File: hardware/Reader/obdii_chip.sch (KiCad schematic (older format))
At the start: 23 parts

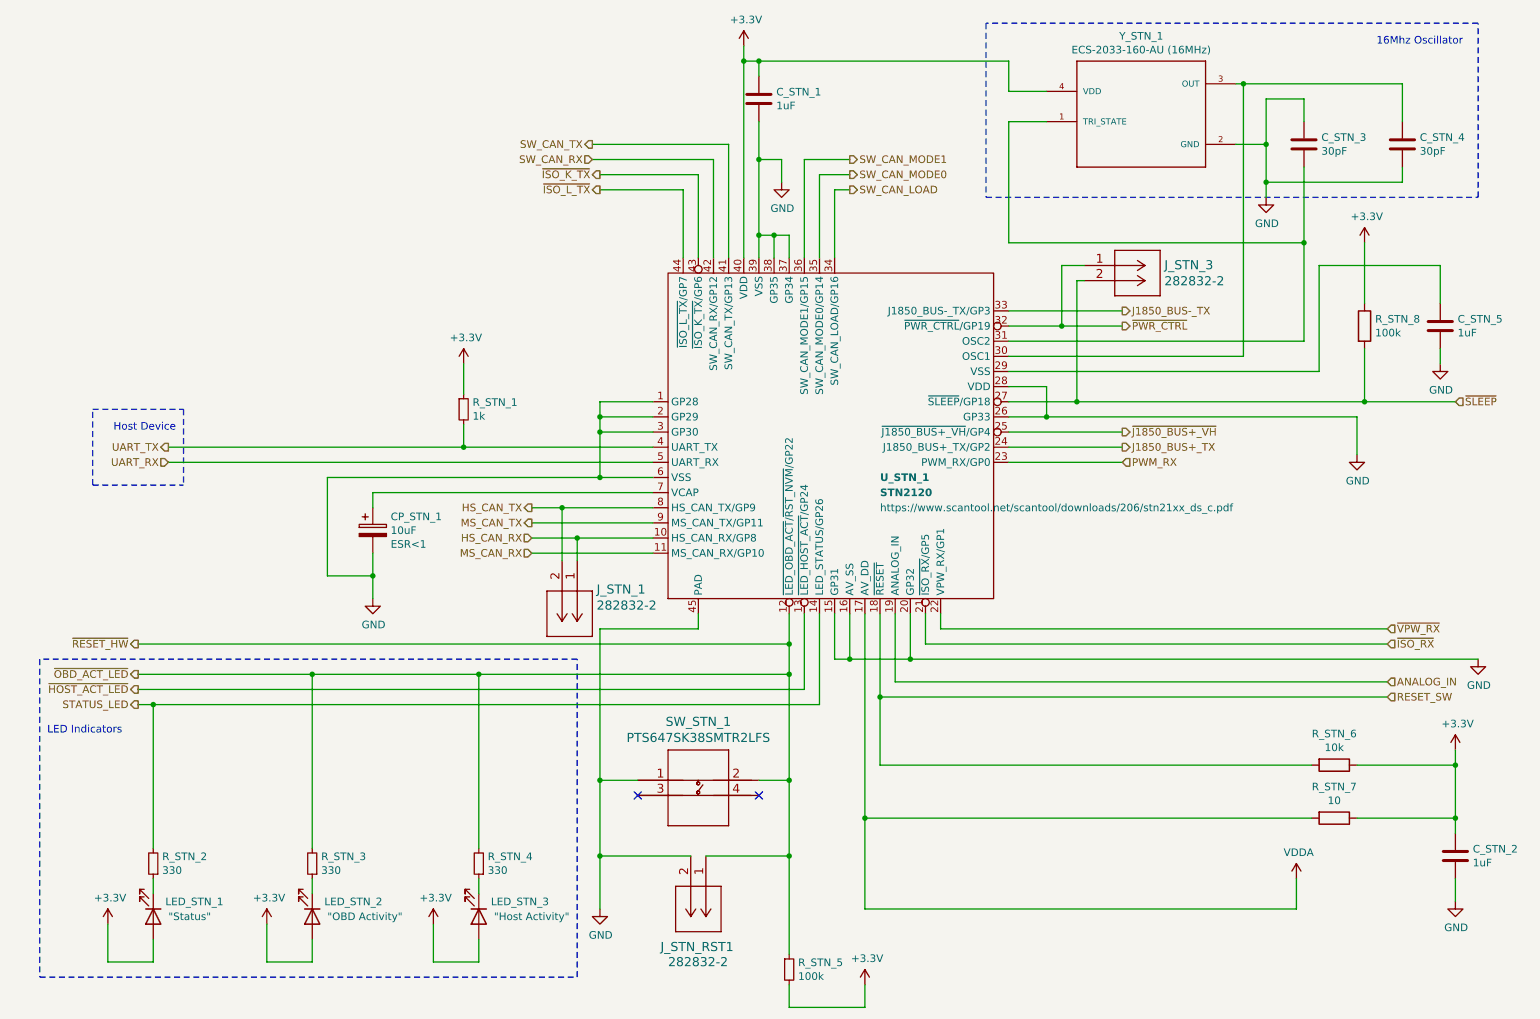
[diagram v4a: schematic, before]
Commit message: Fixed wiring issue on ESD Protection
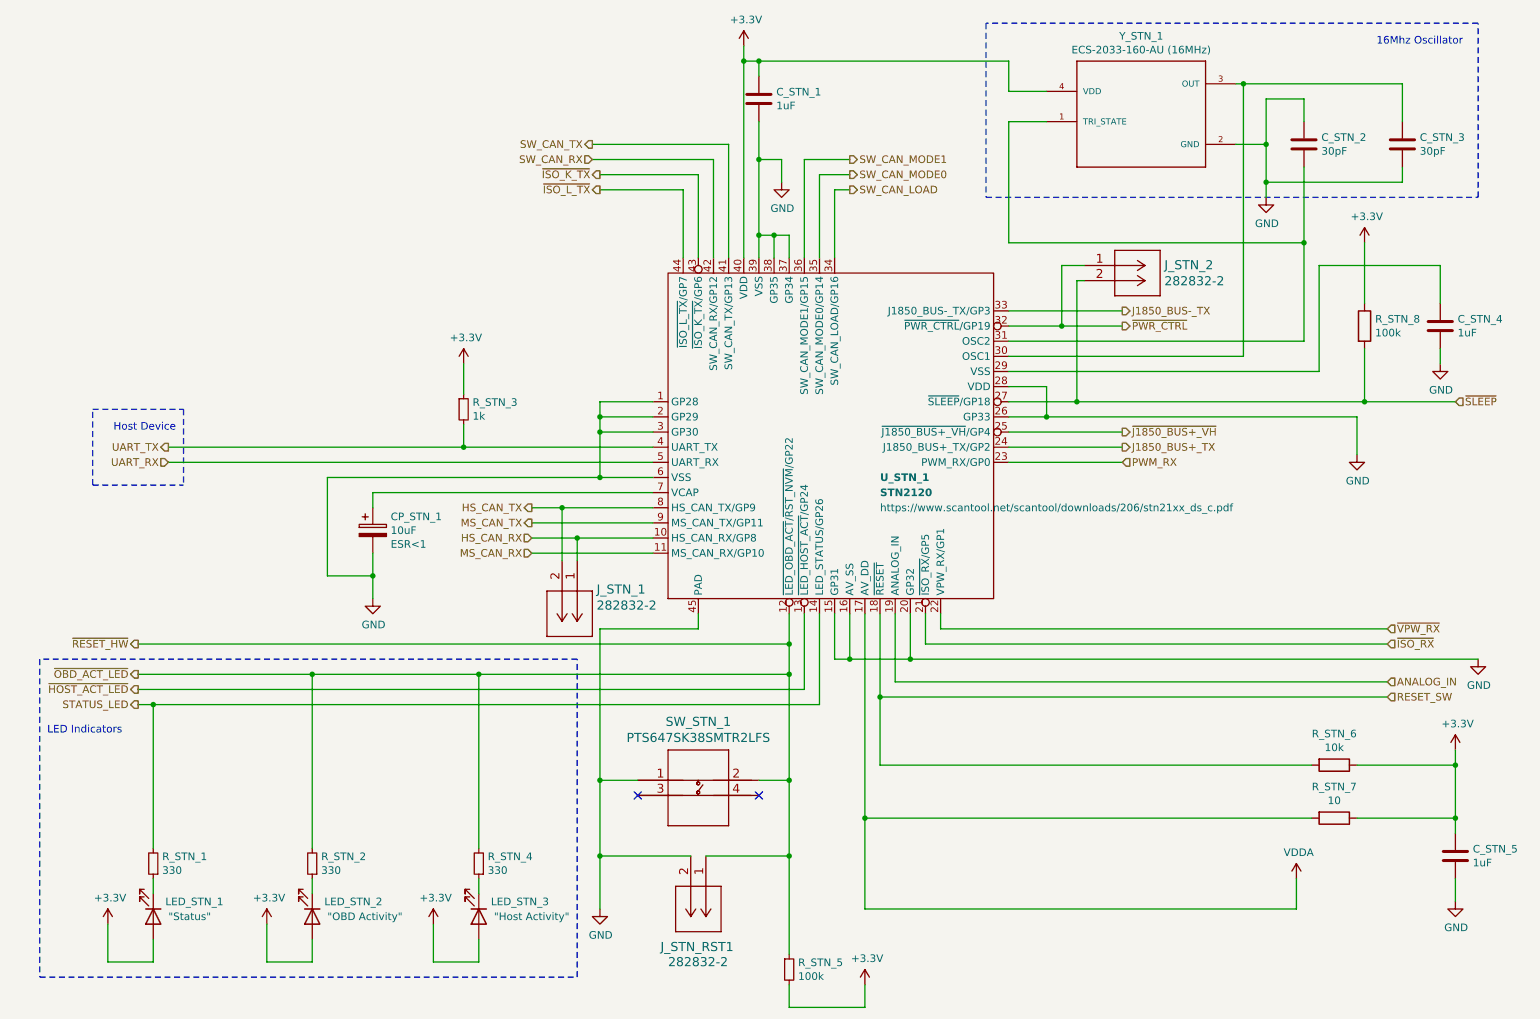
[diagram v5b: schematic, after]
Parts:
- renumbered C_STN_3 to C_STN_2, C_STN_4 to C_STN_3, C_STN_5 to C_STN_4, C_STN_2 to C_STN_5, J_STN_3 to J_STN_2, R_STN_2 to R_STN_1, R_STN_3 to R_STN_2, R_STN_1 to R_STN_3
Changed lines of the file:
@@
 $EndDescr
 $Comp
-L CANtech:STN2120 U?
+L CANtech:STN2120 U_STN_?
 U 1 1 5FC0708B
 P 6050 3350
-AR Path="/5F95F80B/5FC0708B" Ref="U?"  Part="1"
+AR Path="/5F95F80B/5FC0708B" Ref="U_STN_?"  Part="1"
 AR Path="/5F95F80B/5FC0631B/5FC0708B" Ref="U_STN_1"  Part="1"
 F 0 "U_STN_1" H 6250 3000 50  0000 L CNB
@@
 $EndComp
 $Comp
-L Device:R_Small R_STN_1
+L Device:R_Small R_STN_3
 U 1 1 5FC0B04F
 P 3500 3250
-F 0 "R_STN_1" H 3559 3296 50  0000 L CNN
+F 0 "R_STN_3" H 3559 3296 50  0000 L CNN
 F 1 "1k" H 3559 3205 50  0000 L CNN
 F 2 "footprints:RC1608F102CS" H 3500 3250 50  0001 C CNN
@@
 UART_RX
 $Comp
-L power:+3.3V #PWR0192
+L power:+3.3V #PWR060
 U 1 1 5FC0B98A
 P 3500 2950
-F 0 "#PWR0192" H 3500 2800 50  0001 C CNN
+F 0 "#PWR060" H 3500 2800 50  0001 C CNN
 F 1 "+3.3V" H 3515 3123 50  0000 C CNN
 F 2 "" H 3500 2950 50  0001 C CNN
@@
 	4400 3400 4400 3700
 $Comp
-L power:GND #PWR0193
+L power:GND #PWR058
 U 1 1 5FC0D5B0
 P 2900 4500
-F 0 "#PWR0193" H 2900 4250 50  0001 C CNN
+F 0 "#PWR058" H 2900 4250 50  0001 C CNN
 F 1 "GND" H 2905 4327 50  0000 C CNN
 F 2 "" H 2900 4500 50  0001 C CNN
@@
 MS_CAN_RX
 $Comp
-L power:GND #PWR0194
+L power:GND #PWR061
 U 1 1 5FC1071B
 P 4400 6550
-F 0 "#PWR0194" H 4400 6300 50  0001 C CNN
+F 0 "#PWR061" H 4400 6300 50  0001 C CNN
 F 1 "GND" H 4405 6377 50  0000 C CNN
 F 2 "" H 4400 6550 50  0001 C CNN
@@
 $EndComp
 $Comp
-L power:+3.3V #PWR0195
+L power:+3.3V #PWR064
 U 1 1 5FC11757
 P 6150 7050
-F 0 "#PWR0195" H 6150 6900 50  0001 C CNN
+F 0 "#PWR064" H 6150 6900 50  0001 C CNN
 F 1 "+3.3V" H 6165 7223 50  0000 C CNN
 F 2 "" H 6150 7050 50  0001 C CNN
@@
 $EndComp
 $Comp
-L Device:R_Small R_STN_3
+L Device:R_Small R_STN_2
 U 1 1 5FC13627
 P 2500 6250
-F 0 "R_STN_3" H 2441 6204 50  0000 R CNN
+F 0 "R_STN_2" H 2441 6204 50  0000 R CNN
 F 1 "330" H 2441 6295 50  0000 R CNN
 F 2 "footprints:RESC3216X70N" H 2500 6250 50  0001 C CNN
@@
 	2500 6350 2500 6450
 $Comp
-L power:+3.3V #PWR0196
+L power:+3.3V #PWR057
 U 1 1 5FC1B34E
 P 2200 6650
-F 0 "#PWR0196" H 2200 6500 50  0001 C CNN
+F 0 "#PWR057" H 2200 6500 50  0001 C CNN
 F 1 "+3.3V" H 2215 6823 50  0000 C CNN
 F 2 "" H 2200 6650 50  0001 C CNN
@@
 $EndComp
 $Comp
-L Device:R_Small R_STN_2
+L Device:R_Small R_STN_1
 U 1 1 5FC2D134
 P 1450 6250
-F 0 "R_STN_2" H 1391 6204 50  0000 R CNN
+F 0 "R_STN_1" H 1391 6204 50  0000 R CNN
 F 1 "330" H 1391 6295 50  0000 R CNN
 F 2 "footprints:RESC3216X70N" H 1450 6250 50  0001 C CNN
@@
 	1450 6350 1450 6450
 $Comp
-L power:+3.3V #PWR0197
+L power:+3.3V #PWR056
 U 1 1 5FC2D13B
 P 1150 6650
-F 0 "#PWR0197" H 1150 6500 50  0001 C CNN
+F 0 "#PWR056" H 1150 6500 50  0001 C CNN
 F 1 "+3.3V" H 1165 6823 50  0000 C CNN
 F 2 "" H 1150 6650 50  0001 C CNN
@@
 	3600 6350 3600 6450
 $Comp
-L power:+3.3V #PWR0198
+L power:+3.3V #PWR059
 U 1 1 5FC46408
 P 3300 6650
-F 0 "#PWR0198" H 3300 6500 50  0001 C CNN
+F 0 "#PWR059" H 3300 6500 50  0001 C CNN
 F 1 "+3.3V" H 3315 6823 50  0000 C CNN
 F 2 "" H 3300 6650 50  0001 C CNN
@@
 LED Indicators
 $Comp
-L power:GND #PWR0199
+L power:GND #PWR072
 U 1 1 5FC652FD
 P 10200 4900
-F 0 "#PWR0199" H 10200 4650 50  0001 C CNN
+F 0 "#PWR072" H 10200 4650 50  0001 C CNN
 F 1 "GND" H 10205 4727 50  0000 C CNN
 F 2 "" H 10200 4900 50  0001 C CNN
@@
 	7100 3600 7850 3600
 $Comp
-L power:GND #PWR0203
+L power:GND #PWR067
 U 1 1 5FCB385E
 P 9400 3550
-F 0 "#PWR0203" H 9400 3300 50  0001 C CNN
+F 0 "#PWR067" H 9400 3300 50  0001 C CNN
 F 1 "GND" H 9405 3377 50  0000 C CNN
 F 2 "" H 9400 3550 50  0001 C CNN
@@
 $EndComp
 $Comp
-L power:+3.3V #PWR0204
+L power:+3.3V #PWR068
 U 1 1 5FCC6E89
 P 9450 2150
-F 0 "#PWR0204" H 9450 2000 50  0001 C CNN
+F 0 "#PWR068" H 9450 2000 50  0001 C CNN
 F 1 "+3.3V" H 9465 2323 50  0000 C CNN
 F 2 "" H 9450 2150 50  0001 C CNN
@@
 $EndComp
 $Comp
-L Device:C C_STN_5
+L Device:C C_STN_4
 U 1 1 5FCC9B8F
 P 9950 2700
-F 0 "C_STN_5" H 10065 2746 50  0000 L CNN
+F 0 "C_STN_4" H 10065 2746 50  0000 L CNN
 F 1 "1uF" H 10065 2655 50  0000 L CNN
 F 2 "footprints:0603" H 9988 2550 50  0001 C CNN
@@
 $EndComp
 $Comp
-L power:GND #PWR0205
+L power:GND #PWR069
 U 1 1 5FCCCD41
 P 9950 2950
-F 0 "#PWR0205" H 9950 2700 50  0001 C CNN
+F 0 "#PWR069" H 9950 2700 50  0001 C CNN
 F 1 "GND" H 9955 2777 50  0000 C CNN
 F 2 "" H 9950 2950 50  0001 C CNN
@@
 	5250 1500 5250 2250
 $Comp
-L power:+3.3V #PWR0206
+L power:+3.3V #PWR062
 U 1 1 5FCF4C00
 P 5350 850
-F 0 "#PWR0206" H 5350 700 50  0001 C CNN
+F 0 "#PWR062" H 5350 700 50  0001 C CNN
 F 1 "+3.3V" H 5365 1023 50  0000 C CNN
 F 2 "" H 5350 850 50  0001 C CNN
@@
 	5550 2100 5650 2100
 $Comp
-L power:GND #PWR0207
+L power:GND #PWR063
 U 1 1 5FD0B0F8
 P 5600 1750
-F 0 "#PWR0207" H 5600 1500 50  0001 C CNN
+F 0 "#PWR063" H 5600 1500 50  0001 C CNN
 F 1 "GND" H 5605 1577 50  0000 C CNN
 F 2 "" H 5600 1750 50  0001 C CNN
@@
 $EndComp
 $Comp
-L power:GND #PWR0208
+L power:GND #PWR065
 U 1 1 5FE1BF08
 P 8800 1850
-F 0 "#PWR0208" H 8800 1600 50  0001 C CNN
+F 0 "#PWR065" H 8800 1600 50  0001 C CNN
 F 1 "GND" H 8805 1677 50  0000 C CNN
 F 2 "" H 8800 1850 50  0001 C CNN
@@
 $EndComp
 $Comp
-L Device:C C_STN_3
+L Device:C C_STN_2
 U 1 1 5FE374BD
 P 9050 1500
-F 0 "C_STN_3" H 9165 1546 50  0000 L CNN
+F 0 "C_STN_2" H 9165 1546 50  0000 L CNN
 F 1 "30pF" H 9165 1455 50  0000 L CNN
 F 2 "footprints:CAPC1608X90N" H 9088 1350 50  0001 C CNN
@@
 $EndComp
 $Comp
-L Device:C C_STN_4
+L Device:C C_STN_3
 U 1 1 5FE3786D
 P 9700 1500
-F 0 "C_STN_4" H 9815 1546 50  0000 L CNN
+F 0 "C_STN_3" H 9815 1546 50  0000 L CNN
 F 1 "30pF" H 9815 1455 50  0000 L CNN
 F 2 "footprints:CAPC1608X90N" H 9738 1350 50  0001 C CNN
@@
 	4250 4100 4750 4100
 $Comp
-L 2828322:282832-2 J_STN_3
+L 2828322:282832-2 J_STN_2
 U 1 1 5F9BC402
 P 7600 2300
-F 0 "J_STN_3" H 8128 2303 60  0000 L CNN
+F 0 "J_STN_2" H 8128 2303 60  0000 L CNN
 F 1 "282832-2" H 8128 2197 60  0000 L CNN
 F 2 "footprints:282832-2" H 8000 2240 60  0001 C CNN
@@
 	6150 4600 6150 5950
 $Comp
-L power:+3.3V #PWR0200
+L power:+3.3V #PWR070
 U 1 1 5FC68371
 P 10050 5500
-F 0 "#PWR0200" H 10050 5350 50  0001 C CNN
+F 0 "#PWR070" H 10050 5350 50  0001 C CNN
 F 1 "+3.3V" H 10065 5673 50  0000 C CNN
 F 2 "" H 10050 5500 50  0001 C CNN
@@
 $EndComp
 $Comp
-L Device:C C_STN_2
+L Device:C C_STN_5
 U 1 1 5FC6BE46
 P 10050 6200
-F 0 "C_STN_2" H 10165 6246 50  0000 L CNN
+F 0 "C_STN_5" H 10165 6246 50  0000 L CNN
 F 1 "1uF" H 10165 6155 50  0000 L CNN
 F 2 "footprints:0603" H 10088 6050 50  0001 C CNN
@@
 Connection ~ 10050 5600
 $Comp
-L power:GND #PWR0201
+L power:GND #PWR071
 U 1 1 5FC7689D
 P 10050 6500
-F 0 "#PWR0201" H 10050 6250 50  0001 C CNN
+F 0 "#PWR071" H 10050 6250 50  0001 C CNN
 F 1 "GND" H 10055 6327 50  0000 C CNN
 F 2 "" H 10050 6500 50  0001 C CNN
@@
 	10050 6500 10050 6350
 $Comp
-L power:VDDA #PWR0202
+L power:VDDA #PWR066
 U 1 1 5FC78554
 P 9000 6350
-F 0 "#PWR0202" H 9000 6200 50  0001 C CNN
+F 0 "#PWR066" H 9000 6200 50  0001 C CNN
 F 1 "VDDA" H 9015 6523 50  0000 C CNN
 F 2 "" H 9000 6350 50  0001 C CNN
